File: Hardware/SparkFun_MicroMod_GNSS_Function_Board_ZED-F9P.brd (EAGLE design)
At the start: 38 x 65 mm, 191 parts, among them J1 USB Female Type C Connector, J10 U.FL, J11 455-1750-1-ND, J15 QWIIC_VERT, J16 QWIIC_RA, J18 Bus Selection, J2 MICROMOD_STANDARD, J3 Bus Selection, Q1 DMP21D0UT-7, U1 SN74LVC1G66DRYR, U10 SN74AUP1T04, U11 SN74AUP1T04, U2 3.3V, U3 EEPROM, U4 74LVC4066D_QUAD_BILATERAL_SWI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, U5 74LVC4066D_QUAD_BILATERAL_SWI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, U6 OPA344, U7 74LVC541A, U8 U-BLOX_ZED-F9P, U9 FIN1017MX

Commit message: Renamed for release. Some updates post DR.
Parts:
- removed J15: QWIIC_VERT, SparkFun-Connectors:JST04_1MM_VERT
- removed J16: QWIIC_RA, SparkFun-Connectors:JST04_1MM_RA
- removed TP1, TP15, TP16, TP17, TP18, TP19, TP2, TP3, TP4: TEST-POINT3, SparkFun-Connectors:PAD.03X.03
- added R18: 10k, SparkFun-Resistors:0603
- D6: value BLUE -> YELLOW
- J2: value MICROMOD_STANDARD -> MICROMOD_FUNCTION_STANDARD; device SparkFun-MicroMod-Function:M.2-CARD-E-22_FUNCTION_STANDARD -> SparkFun-MicroMod:M.2-CARD-E-22_FUNCTION_STANDARD
- moved JP1 0.30 mm to (32.9, 56.8)
- moved U$101 0.30 mm to (34.9, 56.3)
- moved U$112 0.30 mm to (32.3, 47.8)
- moved U$26 0.30 mm to (32.3, 49.8)
- moved U$57 0.30 mm to (34.3, 40.9)
- moved U$59 0.30 mm to (37.3, 56.3)
- moved U$62 0.30 mm to (32.9, 56.1)
- moved U$63 0.30 mm to (32.3, 51.6)
- moved U$79 0.30 mm to (34.8, 40.9)
- moved U$87 0.30 mm to (33.8, 20.8)
- moved U$88 0.30 mm to (33.9, 17.9)
- moved BT1 0.30 mm to (19.7, 13.2)
- moved C10 0.30 mm to (18.0, 34.1)
- moved C11 0.30 mm to (17.0, 33.1)
- moved C15 0.30 mm to (11.5, 30.4)
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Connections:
- net !RESET!: no longer TP18.1
- net 3.3V: no longer J15.2, J16.2
- net 5V: now also R18.1
- net EXTINT: no longer TP19.1
- net GND: no longer J15.1, J16.1, TP2.1
- net GND_RF: no longer TP4.1
- net MM_SCL: no longer J15.4, J16.4
- net MM_SDA: no longer J15.3, J16.3
- net PWR_EN: now also R18.2
- net RX2/RTCM: no longer TP15.1
- net TX2/RTCM: no longer TP16.1
- net V_BATT: no longer TP3.1
- net V_ZED: no longer TP1.1
- net ZED_!SAFEBOOT!: no longer TP17.1
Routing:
- net MM_SCL: track 45.6 -> 40.9 mm
- net MM_SDA: track 43.9 -> 39.9 mm
- net GND: track 8.47 -> 5.89 mm
- net 3.3V: track 44.6 -> 42.0 mm
- net ZED_!SAFEBOOT!: track 4.79 -> 2.35 mm
- net !RESET!: track 82.5 -> 81.2 mm
- net V_ZED: track 25.1 -> 23.9 mm, vias 19 -> 18
- net RX2/RTCM: track 48.2 -> 47.2 mm
- net TX2/RTCM: track 50.2 -> 49.5 mm
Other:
- board size 38 x 65 mm -> 37.5 x 65 mm

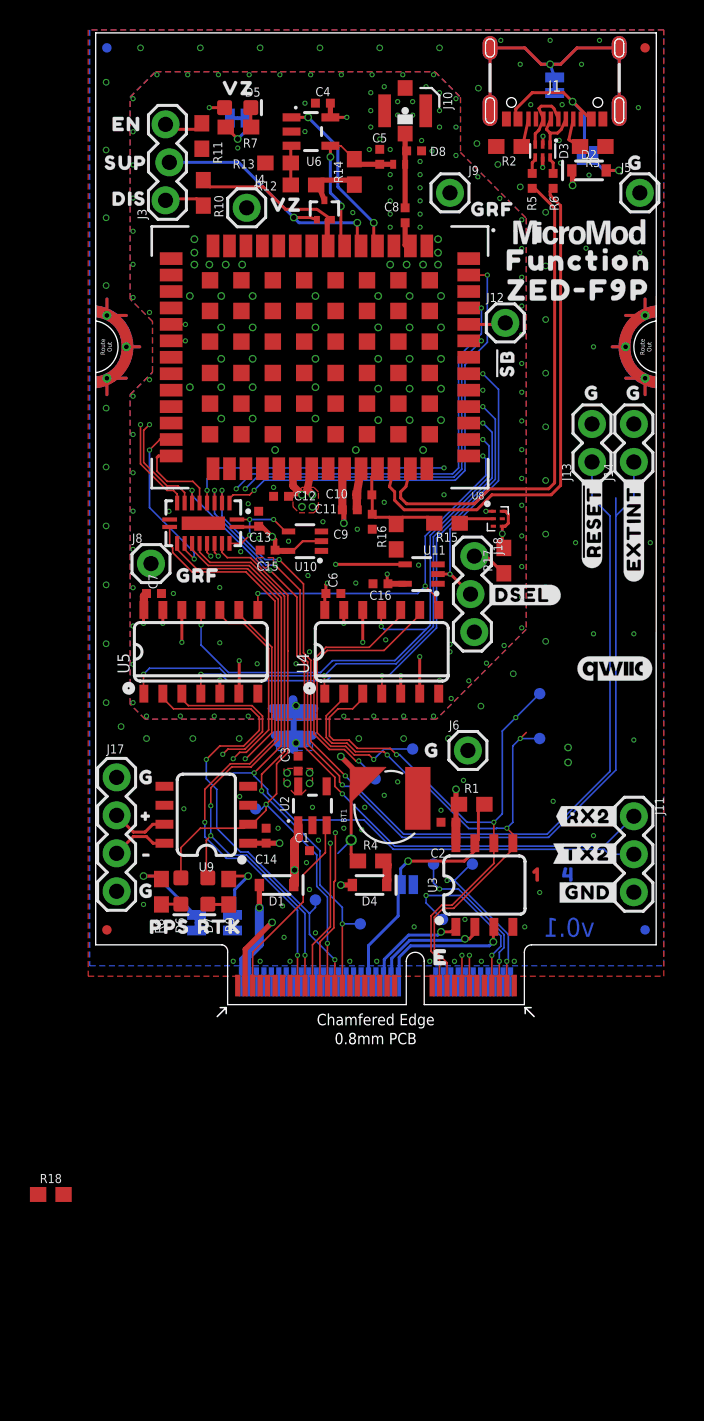
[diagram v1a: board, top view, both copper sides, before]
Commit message: Add part, update lib, resize sch parts, bulk brd update.
Add NLAST SPST switch.
Update POCI/PICO.
Make all resistors possible 0402. (Only 10ohm and 68.1k res are still 0603)
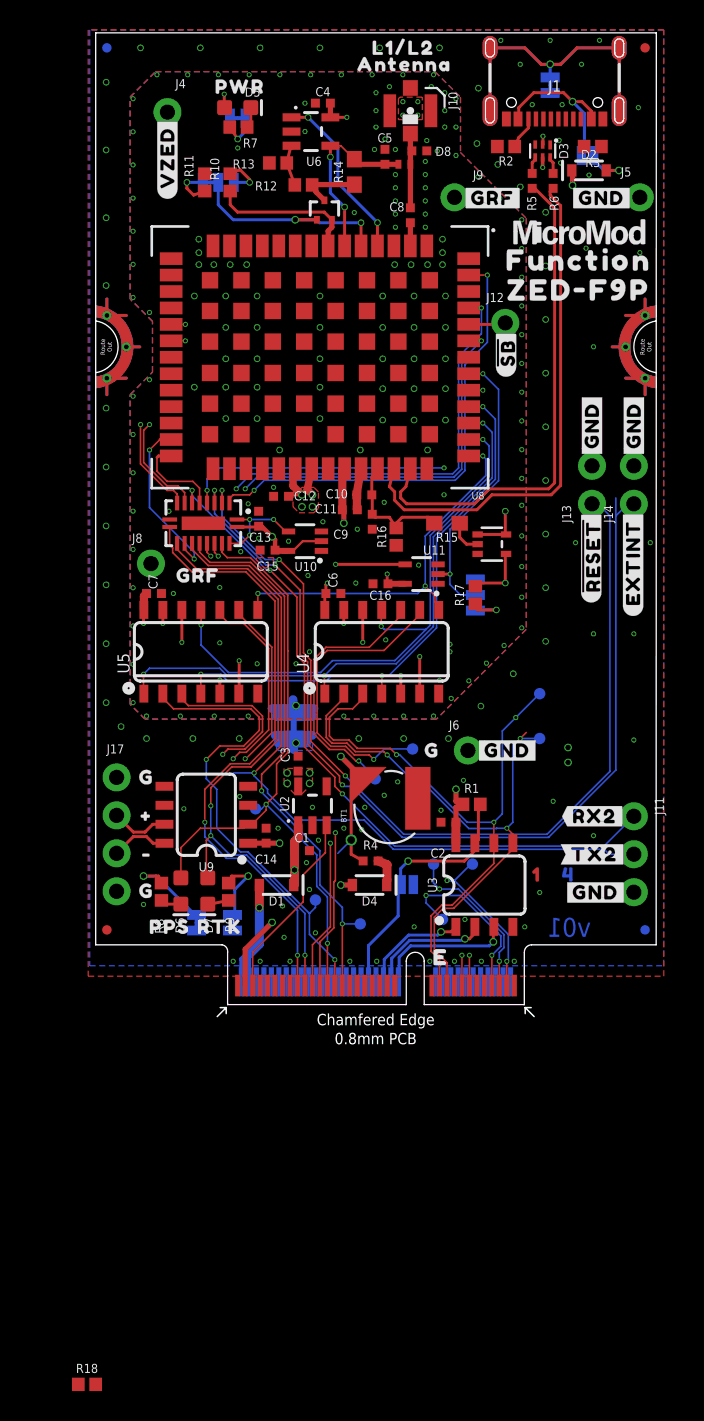
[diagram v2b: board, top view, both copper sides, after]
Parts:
- removed J18, J3: Bus Selection, SparkFun-Connectors:1X03_LOCK
- removed U$101: (no value), output:G2
- removed U$103: (no value), output:#I2C#SER#30
- removed U$107, U$110: (no value), output:EN32
- removed U$108, U$109: (no value), output:DIS33
- removed U$111: (no value), output:SUP35
- removed U$113: (no value), SparkFun-Aesthetics:QWIIC_5MM
- removed U$71: (no value), output:VBATT18
- removed U$81: (no value), output:#DSEL#29
- removed U$84: (no value), output:TX233
- removed U$86: (no value), output:PPS2235
- removed U$88: (no value), output:SDA2237
- removed U$89, U$90: (no value), output:VZ19
- removed U$91: (no value), output:CIPO2240
- removed U$92: (no value), output:SCK2241
- removed U$93: (no value), output:TXR2246
- removed U$94: (no value), output:#CS#2245
- removed U$96: (no value), output:GRF17
- added JP7, JP8: JUMPER-SMT_3_1-NC_TRACE_SILK, SparkFun-Jumpers:SMT-JUMPER_3_1-NC_TRACE_SILK
- C8: device MicroMod_Function_GNSS_ublox_ZED_F9P:0402-TIGHT -> SparkFun_MicroMod_GNSS_Function_Board_ZED-F9P:0402-TIGHT
- J11: device SparkFun-Connectors:1X03 -> SparkFun-Connectors:1X03_NO_SILK
- J12, J4, J5, J6, J8, J9: device SparkFun-Connectors:1X01 -> SparkFun-Connectors:1X01_NO_SILK
- J13, J14: device SparkFun-Connectors:1X02 -> SparkFun-Connectors:1X02_NO_SILK
- J17: device SparkFun-Connectors:1X04 -> SparkFun-Connectors:1X04_NO_SILK
- L1: device MicroMod_Function_GNSS_ublox_ZED_F9P:0402_MURATA -> SparkFun_MicroMod_GNSS_Function_Board_ZED-F9P:0402_MURATA
- Q1: device MicroMod_Function_GNSS_ublox_ZED_F9P:SOT523 -> SparkFun_MicroMod_GNSS_Function_Board_ZED-F9P:SOT523
- R1, R10, R11, R17, R18, R2, R3: device SparkFun-Resistors:0603 -> SparkFun-Resistors:0402
- R12, R7, R8, R9: value 1k -> 1KOHM-0402-1/16W-1%; device SparkFun-Resistors:0603 -> SparkFun-Resistors:0402
- R13, R16: value 100k -> 100K; device SparkFun-Resistors:0603 -> SparkFun-Resistors:0402
- R4: value 3.3k -> 3.3K; device SparkFun-Resistors:0603 -> SparkFun-Resistors:0402-TIGHT
- U$54: device output:#WP#8 -> output:#WP#0
- U$55: device output:G2 -> output:#GRF#0
- U$57, U$58, U$59, U$78, U$79: device output:G2 -> output:#GND#0
- U$66: device output:GRF17 -> output:#I�C#SER#0
- U$67: device output:GRF17 -> output:#GRF#0
- U$68: device output:COPI2239 -> output:#VZED#0
- U$72: device output:VZ4 -> output:PWR0
- U$73: device output:VZ19 -> output:#_DIS#0
- U$74: device output:#ANT_OFF#22 -> output:#EN_#0
- U$75: device output:#VZ#5 -> output:#PWR0
- U$77: device output:WITH_RTK_CORRECTIONS28 -> output:#SUP#0
- U$80: device output:#SB#29 -> output:##SB##0
- U$82: device output:RX231 -> output:#GND#0
- U$83: device output:RX232 -> output:#GND#0
- U$85: device output:TX2234 -> output:L1#L20
- U$87: device output:SCL2236 -> output:ANTENNA0
- U1: value SN74LVC1G66DRYR -> NLAST4501DFT2G; device MicroMod_Function_GNSS_ublox_ZED_F9P:USON_DRY0006A -> SparkFun_MicroMod_GNSS_Function_Board_ZED-F9P:SOT353
- U10, U11: device MicroMod_Function_GNSS_ublox_ZED_F9P:SC-70-5_DCK -> SparkFun_MicroMod_GNSS_Function_Board_ZED-F9P:SC-70-5_DCK
- U7: device MicroMod_Function_GNSS_ublox_ZED_F9P:DHVQFN20 -> SparkFun_MicroMod_GNSS_Function_Board_ZED-F9P:DHVQFN20
- U8: device MicroMod_Function_GNSS_ublox_ZED_F9P:ZED-F9P -> SparkFun_MicroMod_GNSS_Function_Board_ZED-F9P:ZED-F9P
- U9: device MicroMod_Function_GNSS_ublox_ZED_F9P:SO08 -> SparkFun_MicroMod_GNSS_Function_Board_ZED-F9P:SO08
- moved U$85 49.3 mm to (17.8, 64.0), flipped to the top
- moved U$68 47.3 mm to (4.80, 53.9), flipped to the top, turned to 90 degrees
- moved U$87 45.4 mm to (16.8, 62.9), flipped to the top
- moved U$82 42.8 mm to (31.6, 54.0), flipped to the top
- moved U$55 40.7 mm to (24.4, 54.0), flipped to the top
- moved U$66 25.7 mm to (25.4, 35.9), turned to 270 degrees
- moved U$77 17.5 mm to (8.20, 54.3), turned to 270 degrees
- moved R18 12.9 mm to (-0.58, -25.4)
- moved J4 8.31 mm to (4.80, 59.7)
- moved U$58 5.95 mm to (33.2, 36.5), flipped to the top, turned to 90 degrees
- moved U$57 4.72 mm to (36.0, 36.5), flipped to the top, turned to 90 degrees
- moved U$83 4.53 mm to (25.3, 17.0), flipped to the top
- moved U$73 4.37 mm to (6.90, 55.0), flipped to the bottom
- moved U$78 4.00 mm to (36.0, 40.9), flipped to the bottom, turned to 270 degrees
- moved R11 3.11 mm to (7.30, 55.0), turned to 270 degrees
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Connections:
- net MM_CIPO renamed MM_POCI
- net MM_COPI renamed MM_PICO
- net ZED_RX/COPI renamed ZED_RX/PICO
- net ZED_TX/CIPO renamed ZED_TX/POCI
- removed net N$10: J18.1, R17.1
- removed net N$11: J3.1, R10.1
- removed net N$12: J3.3, R11.2
- new net N$1: JP7.1, R10.1
- new net N$2: JP7.3, R11.2
- new net N$5: JP8.3, R17.1
- net !RESET!: now also U7.3; no longer U7.P$3
- net !ZED_DSEL!: now also U11.4; no longer U11.P$4
- net EXTINT: now also U7.4; no longer U7.P$4
- net GEO_STAT: now also U7.11; no longer U7.P$11
- net GND_RF: now also JP8.1, U1.3, U10.3, U11.3, U7.10; no longer J18.3, U1.P$3, U10.P$3, U11.P$3, U7.P$10
- net IO_!OE!: now also U10.4, U7.1, U7.19; no longer U10.P$4, U7.P$1, U7.P$19
- net N$13: now also Q1.1; no longer Q1.P$1
- net N$7: now also L1.2; no longer L1.P$2
- net PPS: now also U7.18; no longer U7.P$18
- net RTK_STAT: now also U7.12; no longer U7.P$12
- net RX2/RTCM: now also U7.7; no longer U7.P$7
- net TX2/RTCM: now also U7.14; no longer U7.P$14
- net TX_READY: now also U7.15; no longer U7.P$15
- net V_RF: now also Q1.2; no longer Q1.P$2
- net V_USB: now also U1.1, U1.5; no longer U1.P$1
- net V_ZED: now also U1.4, U10.2, U10.5, U11.5, U7.20; no longer U1.P$4, U1.P$6, U10.P$2, U10.P$5, U11.P$5, U7.P$20
- net ZED_!RESET!: now also U7.17; no longer U7.P$17
- net ZED_ANT_!SHORT!: now also L1.1; no longer L1.P$1
- net ZED_ANT_OFF: now also JP7.2, Q1.3; no longer J3.2, Q1.P$3
- net ZED_DSEL: now also JP8.2, U11.2; no longer J18.2, U11.P$2
- net ZED_EXTINT: now also U7.16; no longer U7.P$16
- net ZED_GEO_STAT: now also U7.9; no longer U7.P$9
- net ZED_PPS: now also U7.2; no longer U7.P$2
- net ZED_RTK_STAT: now also U7.8; no longer U7.P$8
- net ZED_RX2/RTCM: now also U7.13; no longer U7.P$13
- net ZED_TX2/RTCM: now also U7.6; no longer U7.P$6
- net ZED_TX_READY: now also U7.5; no longer U7.P$5
- net ZED_USB_DET: now also U1.2; no longer U1.P$2
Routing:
- net USBC_P: track 4.54 -> 0.00 mm
- net USBC_N: track 3.51 -> 0.00 mm
- net N$5: track 0.00 -> 3.11 mm, vias 0 -> 1
- net ZED_ANT_OFF: track 17.6 -> 14.5 mm
- net N$2: track 0.00 -> 2.89 mm, vias 0 -> 1
- net N$1: track 0.00 -> 2.88 mm, vias 0 -> 1
- net N$11: track 2.75 -> 0.00 mm
- net N$12: track 2.73 -> 0.00 mm
- net EXTINT: track 83.0 -> 80.4 mm
- net !RESET!: track 81.2 -> 78.7 mm
- net N$10: track 2.45 -> 0.00 mm
- net N$4: track 2.30 -> 0.00 mm
- net V_USB: track 44.7 -> 46.5 mm
- net V_RF: track 11.7 -> 9.99 mm
- net V_ZED: track 23.9 -> 24.8 mm
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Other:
- board text added: "v01"
- board text removed: "v0.1"

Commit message: Completed updates post DR.
Change PPS LED to Yellow.
U1 make power V_USB, not V_ZED.
Add PUR on PWR_EN.
Remove TPs where PTH exists.
Remove Qwiic connectors.
Change U1 to be a bigger package.
Change CIPO/COPI to PICO/POCI.
Route out from center of pad.
Remove silk from PTHs.
Fix skinny VIN trace.
Change 0.2mm vias to 0.3mm vias.
Change 0.35mm vias to 0.3mm vias where possible.
Set layers correctly on board so 2 and 15 are in correct location.
Reset Grid for design.
Change VZ LED silk to PWR.
Change Silk description.
Change i2c silk to have superscript 2.
Change CIPO/COPI to PICO/POCI.
Change version number to v01.
DRC Wire Stubs.
GND pour between power traces on L15.
GND pour between SPI/UART traces on L2.
Acid traps.
Change SS jumpers to SMD jumpers.
Board Dimensions change.
Space out capacitors on board.
Cover ANT with Solder Mask.
Remove copper on L1 from under U.FL.
Write Silk for L1/L2 antenna.
Remove TP silk.
WP Jumper label needs to be rounded on end.
Change names everywhere to SparkFun MicroMod GNSS Function Board - ZED-F9P.
Move U1 origin to center of device.
Remove $ from new FPs.
Text ratio for tDocu.
Changed all passives to 0402 except 10 ohm and 68.1kohm Res.
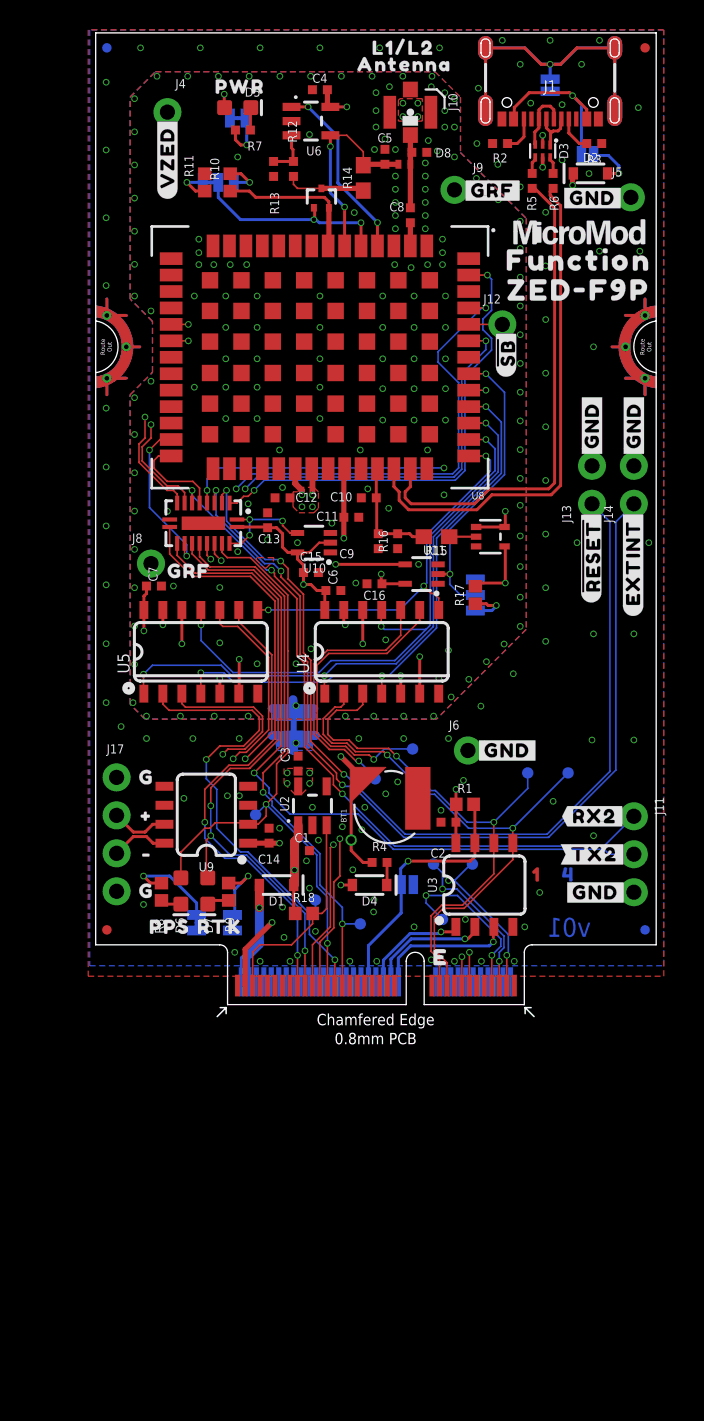
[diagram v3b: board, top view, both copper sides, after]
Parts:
- removed U$102: (no value), output:G2
- JP3: value JUMPER-SMT_2_NC_TRACE_SILK -> JUMPER-SMT_2_NO_SILK; device SparkFun-Jumpers:SMT-JUMPER_2_NC_TRACE_SILK -> SparkFun-Jumpers:SMT-JUMPER_2_NO_SILK
- R12, R7: value 1KOHM-0402-1/16W-1% -> 100k; device SparkFun-Resistors:0402 -> SparkFun-Resistors:0402-TIGHT
- R13, R16: value 100K -> 100k; device SparkFun-Resistors:0402 -> SparkFun-Resistors:0402-TIGHT
- R2, R3: device SparkFun-Resistors:0402 -> SparkFun-Resistors:0402-TIGHT
- moved R18 34.7 mm to (13.9, 6.10)
- moved TP5 5.36 mm to (28.9, 15.5)
- moved C15 3.26 mm to (14.4, 28.9), turned to 0 degrees
- moved TP6 2.98 mm to (31.6, 15.5)
- moved C9 1.36 mm to (18.9, 31.0)
- moved R12 1.26 mm to (13.2, 55.9), turned to 90 degrees
- moved R15 1.14 mm to (22.8, 31.3)
- moved C4 0.92 mm to (15.0, 61.2)
- moved Q1 0.82 mm to (15.1, 53.9)
- moved R14 0.72 mm to (17.9, 55.3)
- moved U6 0.70 mm to (14.4, 59.1)
- moved U$100 0.67 mm to (4.10, 29.0)
- moved C13 0.61 mm to (11.5, 32.4)
- moved U10 0.61 mm to (14.6, 30.9)
- moved R4 0.61 mm to (19.0, 9.51)
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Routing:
- net 3.3V: track 42.5 -> 33.0 mm, vias 5 -> 4
- net V_ZED: track 24.8 -> 29.9 mm, vias 18 -> 16
- net MM_SCL: track 40.9 -> 36.0 mm, vias 3 -> 2
- net USBC_P: track 0.00 -> 4.26 mm
- net USBC_N: track 0.00 -> 3.32 mm
- net GND_RF: track 9.14 -> 6.34 mm, vias 160 -> 158
- net N$4: track 0.00 -> 2.43 mm
- net ZED_EXTINT: track 33.8 -> 35.9 mm
- net MM_SDA: track 39.9 -> 37.9 mm, vias 3 -> 2
- net MM_SCK: track 44.5 -> 46.4 mm
- net 5V: track 63.6 -> 65.4 mm
- net PWR_EN: track 12.8 -> 14.4 mm
- net ZED_ANT_!SHORT!: track 12.2 -> 13.7 mm
- net EXTINT: track 80.4 -> 79.0 mm
- net TX2/RTCM: track 49.5 -> 48.2 mm
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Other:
- outline, holes or cut-outs redrawn
